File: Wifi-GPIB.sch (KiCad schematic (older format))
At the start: 0 parts

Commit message: ESP Serial interface
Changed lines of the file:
@@
 F0 "Power Circuitry" 60
 F1 "power.sch" 60
-F3 "USB_D-" I R 3700 3200 60
-F4 "USB_D+" I R 3700 3350 60
+F3 "USB_D-" I R 3700 3000 60
+F4 "USB_D+" I R 3700 3200 60
 $EndSheet
 $Sheet
@@
 F0 "GPIB and Cortex M0" 60
 F1 "GPIB.sch" 60
-F2 "USB_D-" I L 7350 3200 60
-F3 "USB_D+" I L 7350 3350 60
+F2 "USB_D-" I L 7350 3000 60
+F3 "USB_D+" I L 7350 3200 60
 F4 "ESP_SPI_CS" I L 7350 4100 60
 F5 "ESP_SPI_MOSI" I L 7350 4250 60
@@
 F9 "ESP_GPIO_4" I L 7350 3950 60
 F10 "ESP_GPIO_5" I L 7350 3800 60
+F11 "ESP_RESET" I L 7350 3500 60
 $EndSheet
 $Sheet
@@
 F1 "Wifi.sch" 60
 F2 "ESP_SPI_CLK" I R 5200 7200 60
-F3 "ESP_SPI_MISO" I R 5200 6950 60
-F4 "ESP_SPI_MOSI" I R 5200 6700 60
-F5 "ESP_SPI_CS" I R 5200 6450 60
-F6 "ESP_GPIO4" I R 5200 6200 60
-F7 "ESP_GPIO_5" I R 5200 5950 60
-F8 "ESP_GPIO_16" I R 5200 5700 60
+F3 "ESP_GPIO4" I R 5200 6200 60
+F4 "ESP_GPIO_5" I R 5200 5950 60
+F5 "ESP_GPIO_16" I R 5200 5700 60
+F6 "ESP_RESET" I R 5200 5450 60
+F7 "ESP_SPI_MISO" I R 5200 6950 60
+F8 "ESP_SPI_MOSI/RXD2" I R 5200 6700 60
+F9 "ESP_SPI_CS/TXD2" I R 5200 6450 60
 $EndSheet
-Wire Wire Line
-	3700 3200 7350 3200
-Wire Wire Line
-	3700 3350 7350 3350
 Wire Wire Line
 	5200 5700 5500 5700
@@
 Wire Wire Line
 	6400 4550 7350 4550
+Wire Wire Line
+	7350 3500 5350 3500
+Wire Wire Line
+	5350 3500 5350 5450
+Wire Wire Line
+	5350 5450 5200 5450
+Wire Wire Line
+	7350 3000 3700 3000
+Wire Wire Line
+	7350 3200 3700 3200
 $EndSCHEMATC

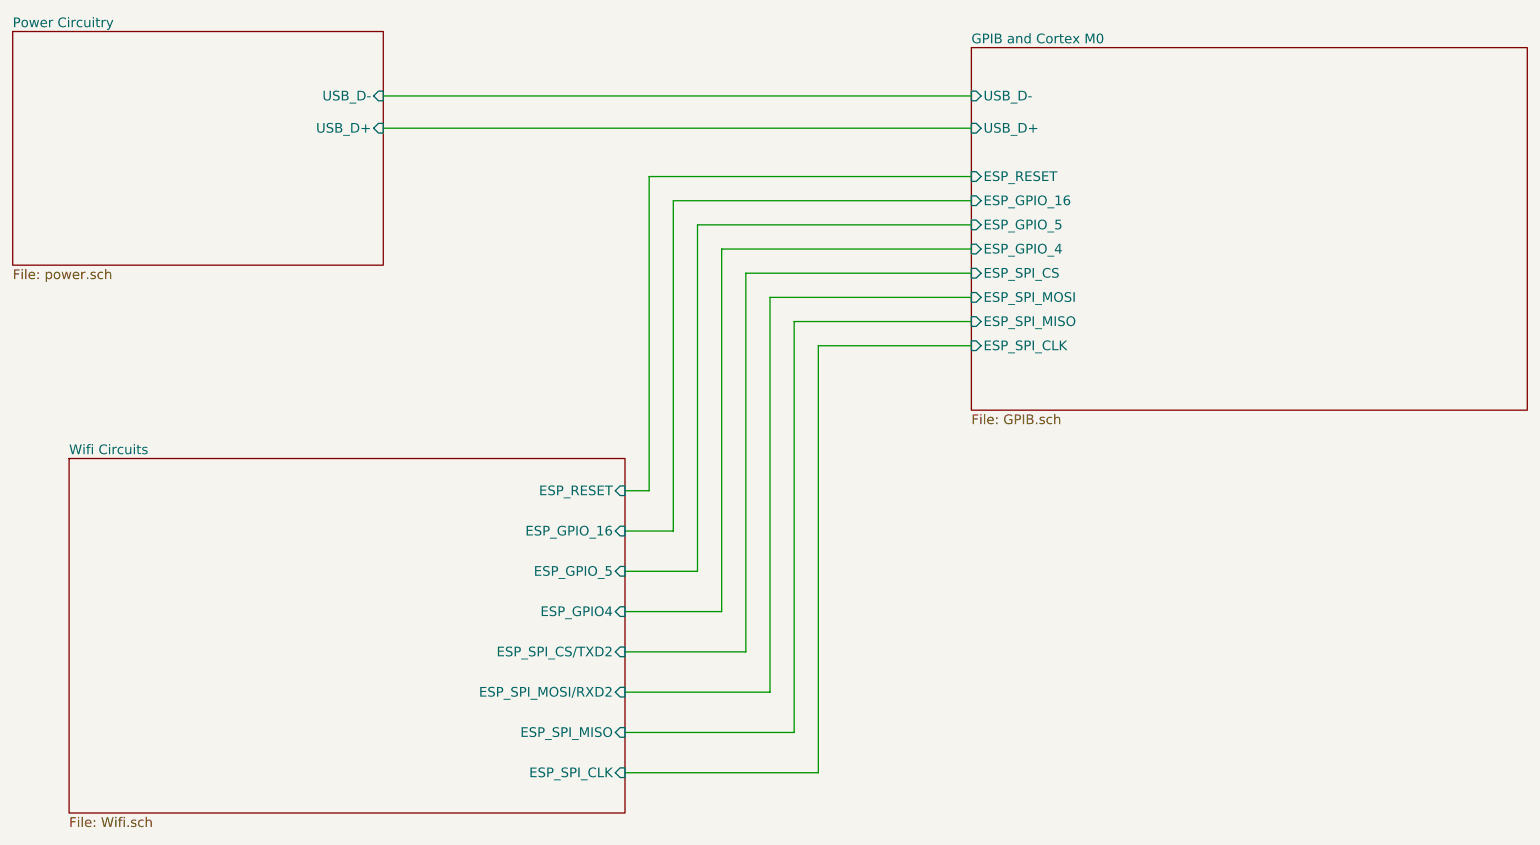
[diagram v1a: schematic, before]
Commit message: ESP doesn't seem to support UART2, switch to UART1
As far as I can tell the TXD2, RXD2 ports are not documented
If they do work, they will only work exclusively of TX1/RX1.
So better to just use the main UART.
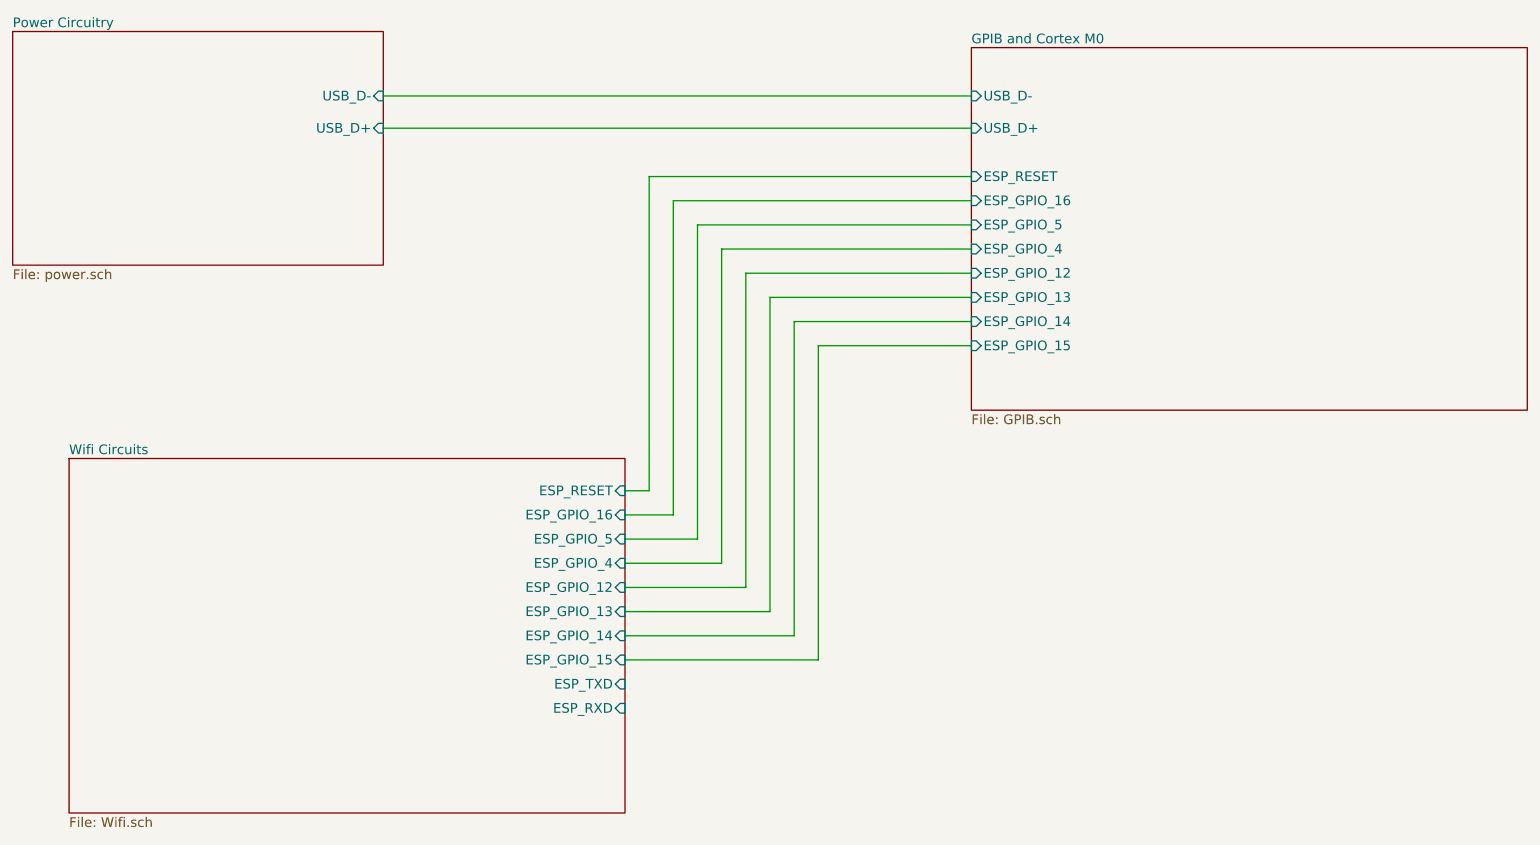
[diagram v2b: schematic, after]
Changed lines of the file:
@@
 F2 "USB_D-" I L 7350 3000 60
 F3 "USB_D+" I L 7350 3200 60
-F4 "ESP_SPI_CS" I L 7350 4100 60
-F5 "ESP_SPI_MOSI" I L 7350 4250 60
-F6 "ESP_SPI_MISO" I L 7350 4400 60
-F7 "ESP_SPI_CLK" I L 7350 4550 60
-F8 "ESP_GPIO_16" I L 7350 3650 60
-F9 "ESP_GPIO_4" I L 7350 3950 60
-F10 "ESP_GPIO_5" I L 7350 3800 60
-F11 "ESP_RESET" I L 7350 3500 60
+F4 "ESP_GPIO_16" I L 7350 3650 60
+F5 "ESP_GPIO_4" I L 7350 3950 60
+F6 "ESP_GPIO_5" I L 7350 3800 60
+F7 "ESP_RESET" I L 7350 3500 60
+F8 "ESP_GPIO_12" I L 7350 4100 60
+F9 "ESP_GPIO_13" I L 7350 4250 60
+F10 "ESP_GPIO_14" I L 7350 4400 60
+F11 "ESP_GPIO_15" I L 7350 4550 60
 $EndSheet
 $Sheet
@@
 F0 "Wifi Circuits" 60
 F1 "Wifi.sch" 60
-F2 "ESP_SPI_CLK" I R 5200 7200 60
-F3 "ESP_GPIO4" I R 5200 6200 60
-F4 "ESP_GPIO_5" I R 5200 5950 60
-F5 "ESP_GPIO_16" I R 5200 5700 60
-F6 "ESP_RESET" I R 5200 5450 60
-F7 "ESP_SPI_MISO" I R 5200 6950 60
-F8 "ESP_SPI_MOSI/RXD2" I R 5200 6700 60
-F9 "ESP_SPI_CS/TXD2" I R 5200 6450 60
+F2 "ESP_GPIO_5" I R 5200 5750 60
+F3 "ESP_GPIO_16" I R 5200 5600 60
+F4 "ESP_RESET" I R 5200 5450 60
+F5 "ESP_TXD" I R 5200 6650 60
+F6 "ESP_RXD" I R 5200 6800 60
+F7 "ESP_GPIO_4" I R 5200 5900 60
+F8 "ESP_GPIO_14" I R 5200 6350 60
+F9 "ESP_GPIO_12" I R 5200 6050 60
+F10 "ESP_GPIO_13" I R 5200 6200 60
+F11 "ESP_GPIO_15" I R 5200 6500 60
 $EndSheet
 Wire Wire Line
-	5200 5700 5500 5700
+	5200 5600 5500 5600
 Wire Wire Line
-	5500 5700 5500 3650
+	5500 5600 5500 3650
 Wire Wire Line
 	5500 3650 7350 3650
 Wire Wire Line
-	5200 5950 5650 5950
+	5200 5750 5650 5750
 Wire Wire Line
-	5650 5950 5650 3800
+	5650 5750 5650 3800
 Wire Wire Line
 	5650 3800 7350 3800
 Wire Wire Line
-	5200 6200 5800 6200
+	5200 5900 5800 5900
 Wire Wire Line
-	5800 6200 5800 3950
+	5800 5900 5800 3950
 Wire Wire Line
 	5800 3950 7350 3950
 Wire Wire Line
-	5200 6450 5950 6450
+	5200 6050 5950 6050
 Wire Wire Line
-	5950 6450 5950 4100
+	5950 6050 5950 4100
 Wire Wire Line
 	5950 4100 7350 4100
 Wire Wire Line
-	5200 6700 6100 6700
+	5200 6200 6100 6200
 Wire Wire Line
-	6100 6700 6100 4250
+	6100 6200 6100 4250
 Wire Wire Line
 	6100 4250 7350 4250
 Wire Wire Line
-	5200 6950 6250 6950
+	5200 6350 6250 6350
 Wire Wire Line
-	6250 6950 6250 4400
+	6250 6350 6250 4400
 Wire Wire Line
 	6250 4400 7350 4400
 Wire Wire Line
-	5200 7200 6400 7200
+	5200 6500 6400 6500
 Wire Wire Line
-	6400 7200 6400 4550
+	6400 6500 6400 4550
 Wire Wire Line
 	6400 4550 7350 4550

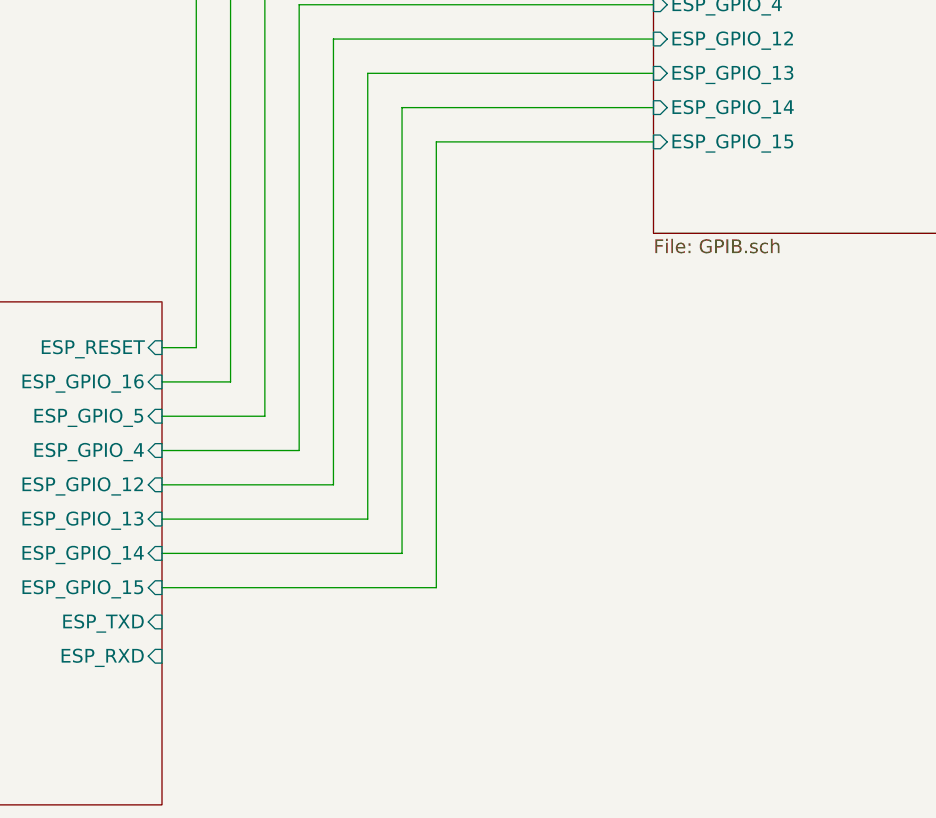
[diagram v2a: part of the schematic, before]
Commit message: DRCs mostly fixed
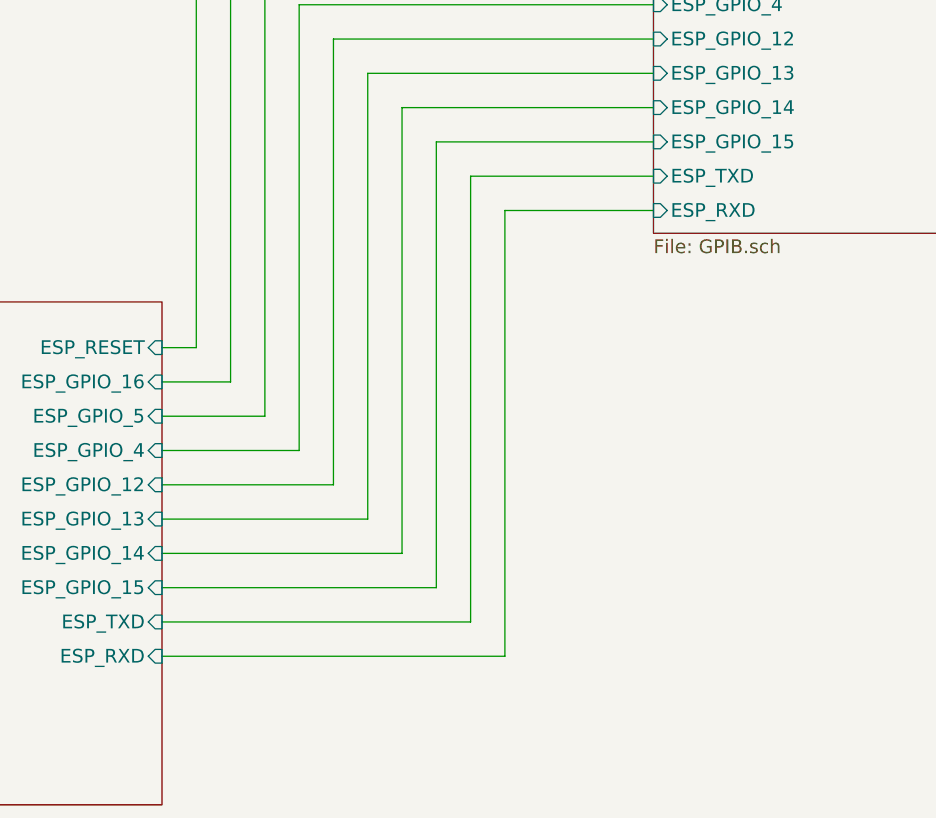
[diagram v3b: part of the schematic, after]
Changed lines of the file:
@@
 F10 "ESP_GPIO_14" I L 7350 4400 60
 F11 "ESP_GPIO_15" I L 7350 4550 60
+F12 "ESP_TXD" I L 7350 4700 60
+F13 "ESP_RXD" I L 7350 4850 60
 $EndSheet
 $Sheet
@@
 Wire Wire Line
 	7350 3200 3700 3200
+Wire Wire Line
+	7350 4700 6550 4700
+Wire Wire Line
+	6550 4700 6550 6650
+Wire Wire Line
+	6550 6650 5200 6650
+Wire Wire Line
+	5200 6800 6700 6800
+Wire Wire Line
+	6700 6800 6700 4850
+Wire Wire Line
+	6700 4850 7350 4850
 $EndSCHEMATC
